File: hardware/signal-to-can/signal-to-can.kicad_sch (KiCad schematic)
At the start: 0 parts

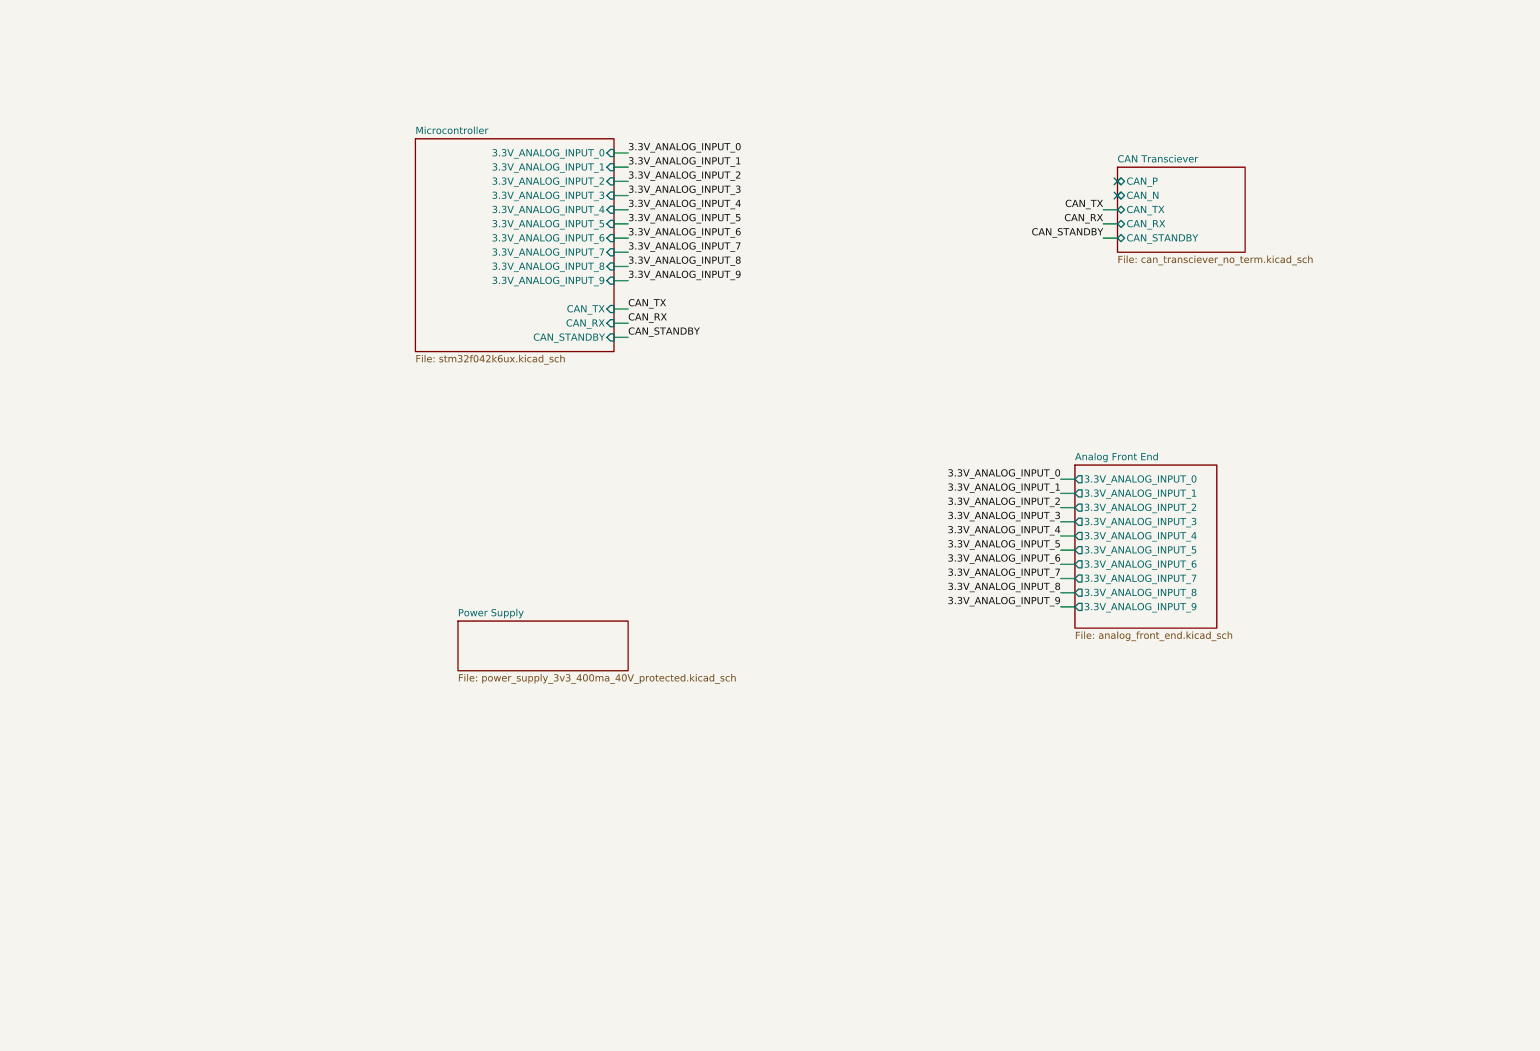
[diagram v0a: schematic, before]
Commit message: AFE, power supply, connector
Ready for PCB layout
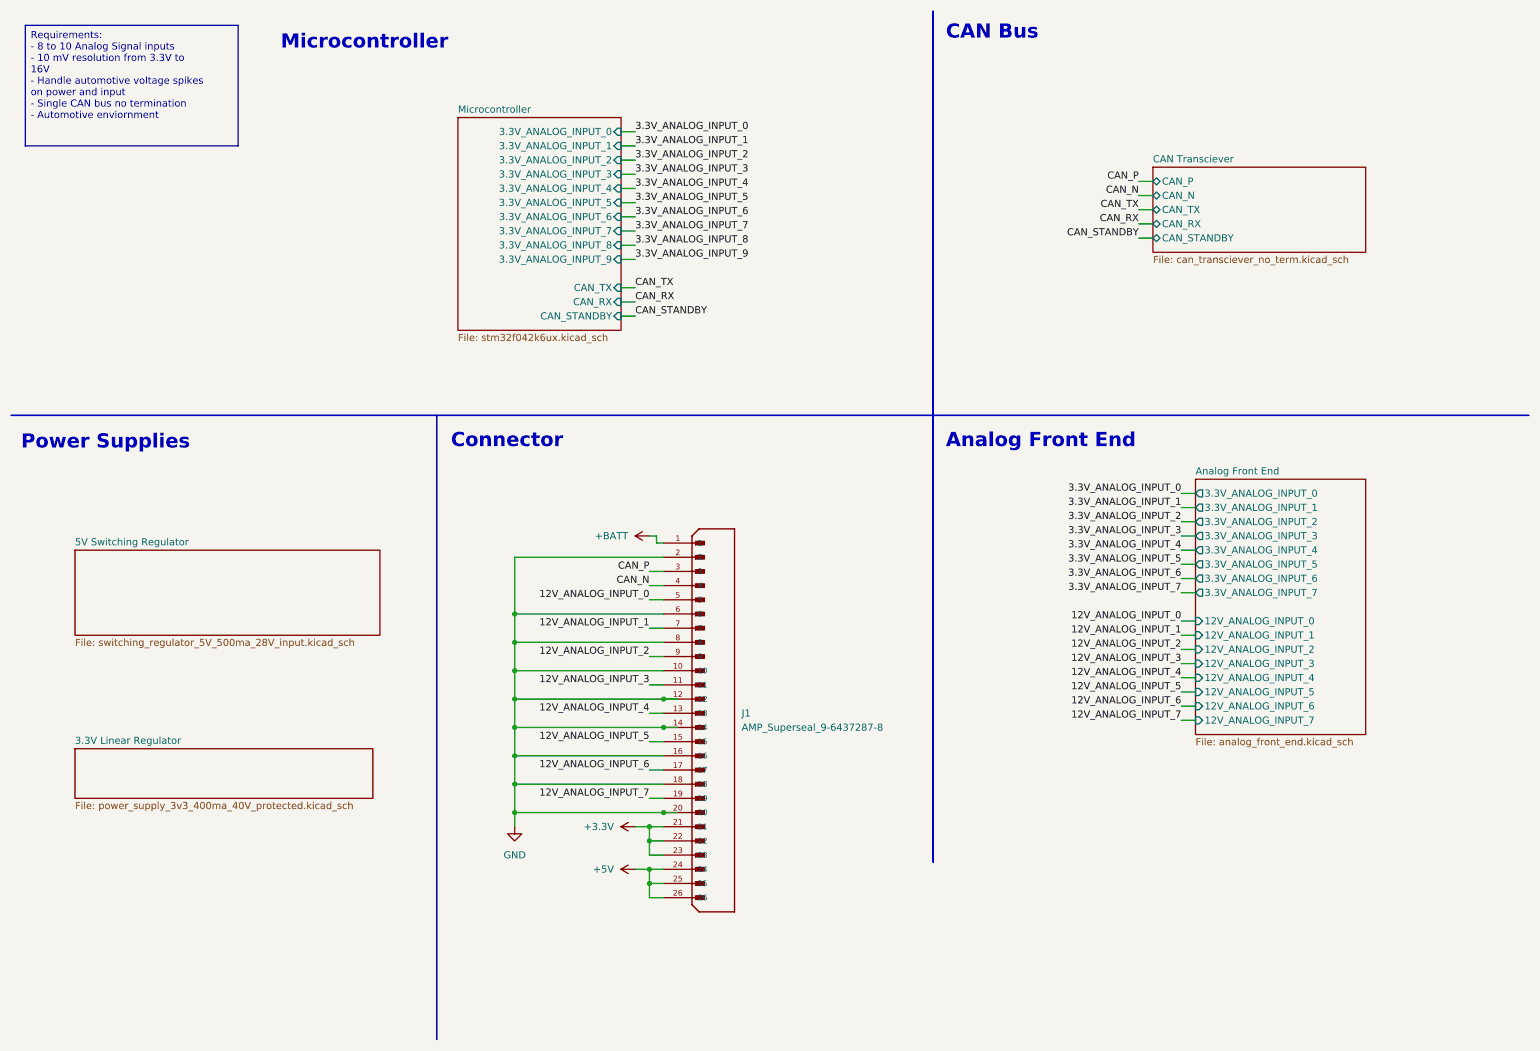
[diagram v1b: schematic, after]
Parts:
- added J1: AMP_Superseal_9-6437287-8, can_datalogger_board:TE_9-6437287-8, symbol signal-to-can:AMP_Superseal_9-6437287-8
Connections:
- new net +3.3V: J1.21, J1.22, J1.23
- new net +5V: J1.24, J1.25, J1.26
- new net +BATT: J1.1
- new net 12V_ANALOG_INPUT_0: J1.5
- new net 12V_ANALOG_INPUT_1: J1.7
- new net 12V_ANALOG_INPUT_2: J1.9
- new net 12V_ANALOG_INPUT_3: J1.11
- new net 12V_ANALOG_INPUT_4: J1.13
- new net 12V_ANALOG_INPUT_5: J1.15
- new net 12V_ANALOG_INPUT_6: J1.17
- new net 12V_ANALOG_INPUT_7: J1.19
- new net CAN_N: J1.4
- new net CAN_P: J1.3
- new net GND: J1.10, J1.12, J1.14, J1.16, J1.18, J1.2, J1.20, J1.6, J1.8
- no-connect marks 2 -> 0
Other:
- sheet Power Supply renamed 3.3V Linear Regulator
- added sheet 5V Switching Regulator (switching_regulator_5V_500ma_28V_input.kicad_sch)
- sheet Analog Front End ports: added 12V_ANALOG_INPUT_0, 12V_ANALOG_INPUT_1, 12V_ANALOG_INPUT_2, 12V_ANALOG_INPUT_3, 12V_ANALOG_INPUT_4, 12V_ANALOG_INPUT_5, 12V_ANALOG_INPUT_6, 12V_ANALOG_INPUT_7; removed 3.3V_ANALOG_INPUT_8, 3.3V_ANALOG_INPUT_9
- note added: "Analog Front End"
- note added: "CAN Bus"
- note added: "Connector"
- note added: "Microcontroller"
- note added: "Power Supplies"
- company: (none) -> Brian Glen
- title: (none) -> Signal to CAN Device

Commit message: 1st rev PCB layout
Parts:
- added H1, H2, H3, H4: MountingHole, MountingHole:MountingHole_3.2mm_M3, symbol Mechanical:MountingHole
- J1: footprint can_datalogger_board:TE_9-6437287-8 -> signal_to_can:TE_9-6437287-8_1
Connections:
- net +3.3V: now also J1.17, J1.18, J1.19; no longer J1.21, J1.22, J1.23
- net +5V: now also J1.23; no longer J1.26
- net +BATT: now also J1.26; no longer J1.1
- net 12V_ANALOG_INPUT_0: now also J1.7; no longer J1.5
- net 12V_ANALOG_INPUT_1: now also J1.6; no longer J1.7
- net 12V_ANALOG_INPUT_2: now also J1.5; no longer J1.9
- net 12V_ANALOG_INPUT_3: now also J1.4; no longer J1.11
- net 12V_ANALOG_INPUT_4: now also J1.3; no longer J1.13
- net 12V_ANALOG_INPUT_5: now also J1.2; no longer J1.15
- net 12V_ANALOG_INPUT_6: now also J1.16; no longer J1.17
- net 12V_ANALOG_INPUT_7: now also J1.15; no longer J1.19
- net CAN_N: now also J1.14; no longer J1.4
- net CAN_P: now also J1.20; no longer J1.3
- net GND: now also J1.1, J1.11, J1.13, J1.21, J1.22, J1.9; no longer J1.14, J1.16, J1.18, J1.2, J1.20, J1.6
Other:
- sheet Microcontroller ports: added none; removed 3.3V_ANALOG_INPUT_8, 3.3V_ANALOG_INPUT_9
- moved on the sheet: J1

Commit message: production v1
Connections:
- net +3.3V renamed +3V3
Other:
- note added: "PCB Header: 9-6437287-8 - 26 pin, 4 row - keying type: 1 - locking type: upper Mating Part: 3-1437290-7 Mating Part terminals: 3-1447221-3 (18-22 awg) Cavity Plug: 4-1437284-3"
- moved on the sheet: J1
